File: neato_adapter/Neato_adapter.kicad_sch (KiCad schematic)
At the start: 9 parts, among them J1 JST PH B4B Vert, J2 JST PH B2B Vert, J3 JST PH B4B Vert, Q1 AS2302, U1 DNP LM2596

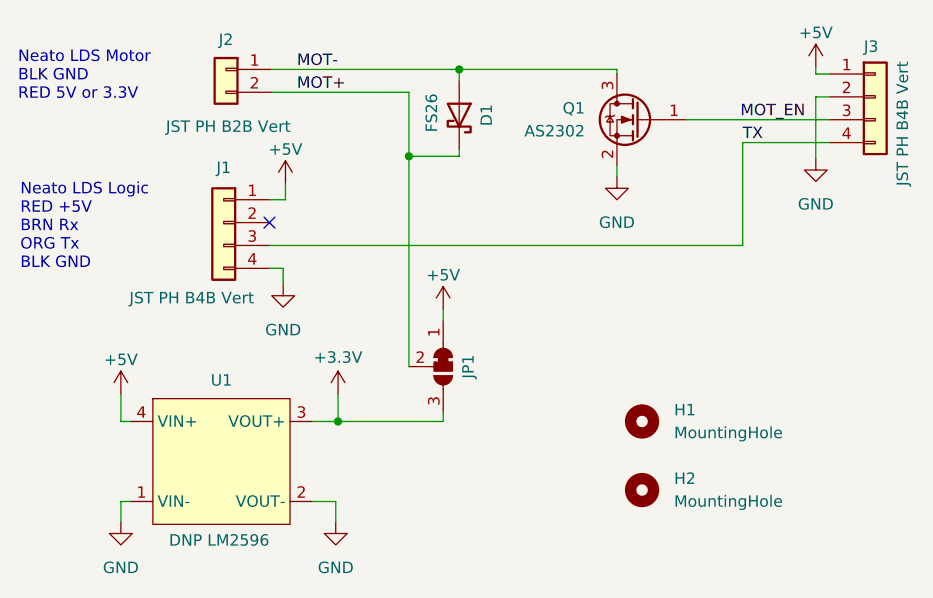
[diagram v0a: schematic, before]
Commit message: Neato, LDS02RR v0.2.0
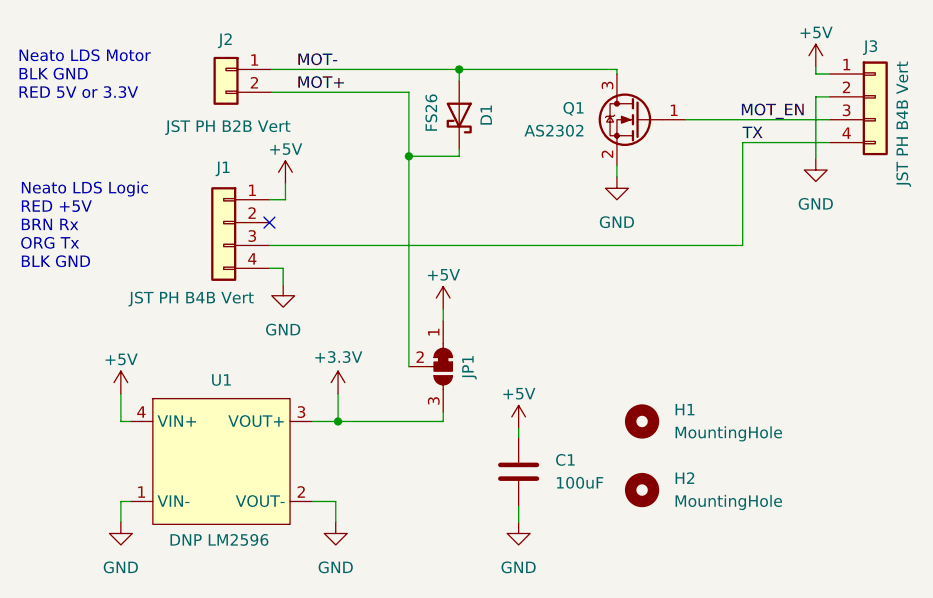
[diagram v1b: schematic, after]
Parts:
- added C1: 100uF, Capacitor_SMD:C_1206_3216Metric, symbol Device:C
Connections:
- net +5V: now also C1.1
- net GND: now also C1.2
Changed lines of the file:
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@@
   (title_block
     (title "Neato XV/Botvac LDS adapter")
-    (date "2024-01-16")
-    (rev "0.1.0")
+    (date "2024-01-30")
+    (rev "0.2.0")
     (company "makerspet.com")
   )
@@
     (stroke (width 0) (type default))
   )
+  (wire (pts (xy 99.568 74.676) (xy 99.568 75.692))
+    (stroke (width 0) (type default))
+  )
   (wire (pts (xy 73.66 49.276) (xy 71.882 49.276))
     (stroke (width 0) (type default))
@@
   )
   (wire (pts (xy 92.964 44.45) (xy 87.376 44.45))
+    (stroke (width 0) (type default))
+  )
+  (wire (pts (xy 99.568 85.09) (xy 99.568 83.312))
     (stroke (width 0) (type default))
   )
@@
     )
   )
+  (symbol (lib_id "power:GND") (at 99.568 85.09 0) (unit 1)
+    (in_bom yes) (on_board yes) (dnp no) (fields_autoplaced)
+    (property "Reference" "#PWR012" (at 99.568 91.44 0)
+      (effects (font (size 1.27 1.27)) hide)
+    )
+    (property "Value" "GND" (at 99.568 90.17 0)
+      (effects (font (size 1.27 1.27)))
+    )
+    (property "Footprint" "" (at 99.568 85.09 0)
+      (effects (font (size 1.27 1.27)) hide)
+    )
+    (property "Datasheet" "" (at 99.568 85.09 0)
+      (effects (font (size 1.27 1.27)) hide)
+    )
+    (pin "1")
+    (instances
+      (project "Neato_adapter"
+        (path "/c13da21a-388e-44a0-831a-aa3d56cf7c53"
+          (reference "#PWR012") (unit 1)
+        )
+      )
+      (project "esp32_breakout"
+        (path "/e24ae185-8f18-408c-aee8-f727519bade3"
+          (reference "#PWR011") (unit 1)
+        )
+      )
+    )
+  )
   (symbol (lib_id "power:+5V") (at 91.186 61.468 0) (unit 1)
     (in_bom yes) (on_board yes) (dnp no) (fields_autoplaced)
@@
         (path "/e24ae185-8f18-408c-aee8-f727519bade3"
           (reference "#PWR011") (unit 1)
+        )
+      )
+    )
+  )
+  (symbol (lib_id "Device:C") (at 99.568 79.502 0) (unit 1)
+    (in_bom yes) (on_board yes) (dnp no) (fields_autoplaced)
+    (property "Reference" "C1" (at 103.632 78.232 0)
+      (effects (font (size 1.27 1.27)) (justify left))
+    )
+    (property "Value" "100uF" (at 103.632 80.772 0)
+      (effects (font (size 1.27 1.27)) (justify left))
+    )
+    (property "Footprint" "Capacitor_SMD:C_1206_3216Metric" (at 100.5332 83.312 0)
+      (effects (font (size 1.27 1.27)) hide)
+    )
+    (property "Datasheet" "~" (at 99.568 79.502 0)
+      (effects (font (size 1.27 1.27)) hide)
+    )
+    (pin "1")
+    (pin "2")
+    (instances
+      (project "Neato_adapter"
+        (path "/c13da21a-388e-44a0-831a-aa3d56cf7c53"
+          (reference "C1") (unit 1)
         )
       )
@@
         )
       )
+    )
+  )
+  (symbol (lib_id "power:+5V") (at 99.568 74.676 0) (unit 1)
+    (in_bom yes) (on_board yes) (dnp no) (fields_autoplaced)
+    (property "Reference" "#PWR01" (at 99.568 78.486 0)
+      (effects (font (size 1.27 1.27)) hide)
+    )
+    (property "Value" "+5V" (at 99.568 70.866 0)
+      (effects (font (size 1.27 1.27)))
+    )
+    (property "Footprint" "" (at 99.568 74.676 0)
+      (effects (font (size 1.27 1.27)) hide)
+    )
+    (property "Datasheet" "" (at 99.568 74.676 0)
+      (effects (font (size 1.27 1.27)) hide)
+    )
+    (pin "1")
+    (instances
+      (project "Neato_adapter"
+        (path "/c13da21a-388e-44a0-831a-aa3d56cf7c53"
+          (reference "#PWR01") (unit 1)
+        )
+      )
+      (project "esp32_breakout"
+        (path "/e24ae185-8f18-408c-aee8-f727519bade3"
+          (reference "#PWR012") (unit 1)
+        )
+      )
